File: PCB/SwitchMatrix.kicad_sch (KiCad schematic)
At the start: 94 parts, among them K1 KEYSW, K10 KEYSW, K11 KEYSW, K12 KEYSW, K13 KEYSW, K14 KEYSW, K15 KEYSW, K16 KEYSW, K17 KEYSW, K18 KEYSW, K19 KEYSW, K2 KEYSW, K20 KEYSW, K21 KEYSW, K22 KEYSW, K23 KEYSW, K24 KEYSW, K25 KEYSW, K26 KEYSW, K27 KEYSW, K28 KEYSW, K29 KEYSW, K3 KEYSW, K30 KEYSW, K31 KEYSW, K32 KEYSW, K33 KEYSW, K34 KEYSW, K35 KEYSW, K36 KEYSW, K37 KEYSW, K38 KEYSW, K39 KEYSW, K4 KEYSW, K40 KEYSW, K41 KEYSW, K42 KEYSW, K43 KEYSW, K44 KEYSW, K45 KEYSW, K46 KEYSW, K47 KEYSW, K5 KEYSW, K6 KEYSW, K7 KEYSW, K8 KEYSW, K9 KEYSW

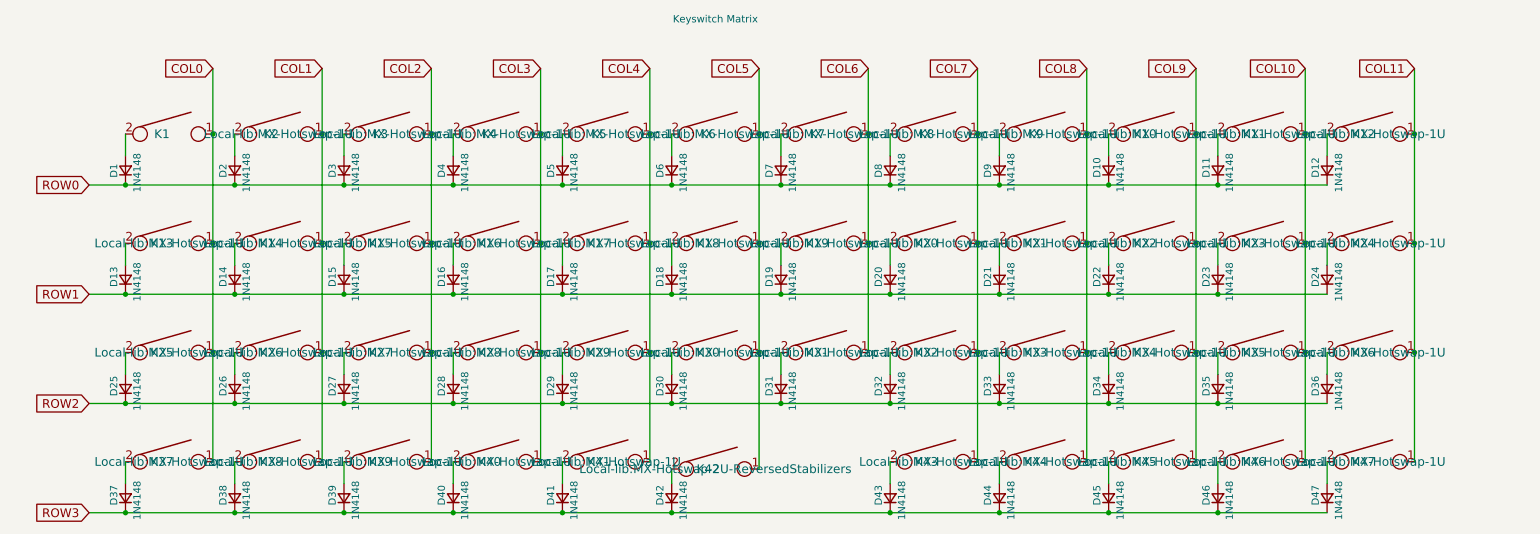
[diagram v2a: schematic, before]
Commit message: update 1u footprints adjust spacing
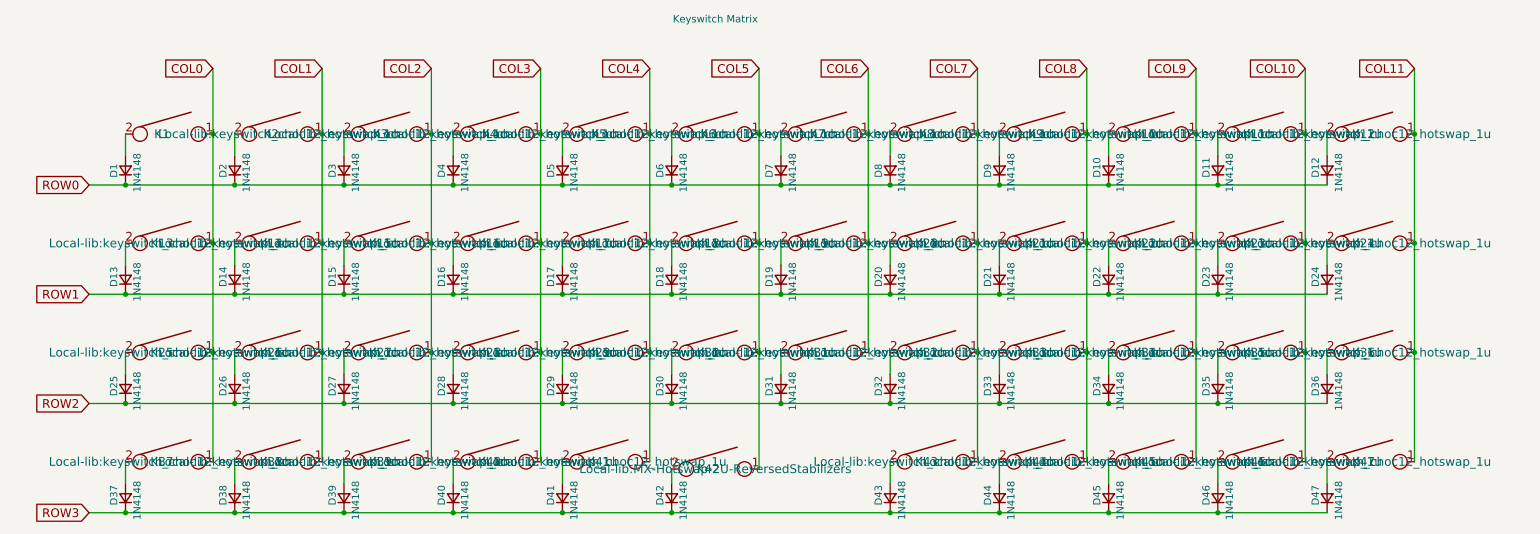
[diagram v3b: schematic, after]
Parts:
- K1, K10, K11, K12, K13, K14, K15, K16, K17, K18, K19, K2, K20, K21, K22, K23, K24, K25, K26, K27, K28, K29, K3, K30, K31, K32, K33, K34, K35, K36, K37, K38, K39, K4, K40, K41, K43, K44, K45, K46, K47, K5, K6, K7, K8, K9: footprint Local-lib:MX-Hotswap-1U -> Local-lib:keyswitch_choc12_hotswap_1u
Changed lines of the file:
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@@
 			)
 		)
-		(property "Footprint" "Local-lib:MX-Hotswap-1U"
+		(property "Footprint" "Local-lib:keyswitch_choc12_hotswap_1u"
 			(at 204.47 124.46 0)
 			(show_name no)
@@
 			)
 		)
-		(property "Footprint" "Local-lib:MX-Hotswap-1U"
+		(property "Footprint" "Local-lib:keyswitch_choc12_hotswap_1u"
 			(at 90.17 105.41 0)
 			(show_name no)
@@
 			)
 		)
-		(property "Footprint" "Local-lib:MX-Hotswap-1U"
+		(property "Footprint" "Local-lib:keyswitch_choc12_hotswap_1u"
 			(at 166.37 105.41 0)
 			(show_name no)
@@
 			)
 		)
-		(property "Footprint" "Local-lib:MX-Hotswap-1U"
+		(property "Footprint" "Local-lib:keyswitch_choc12_hotswap_1u"
 			(at 90.17 86.36 0)
 			(show_name no)
@@
 			)
 		)
-		(property "Footprint" "Local-lib:MX-Hotswap-1U"
+		(property "Footprint" "Local-lib:keyswitch_choc12_hotswap_1u"
 			(at 52.07 86.36 0)
 			(show_name no)
@@
 			)
 		)
-		(property "Footprint" "Local-lib:MX-Hotswap-1U"
+		(property "Footprint" "Local-lib:keyswitch_choc12_hotswap_1u"
 			(at 261.62 105.41 0)
 			(show_name no)
@@
 			)
 		)
-		(property "Footprint" "Local-lib:MX-Hotswap-1U"
+		(property "Footprint" "Local-lib:keyswitch_choc12_hotswap_1u"
 			(at 71.12 67.31 0)
 			(show_name no)
@@
 			)
 		)
-		(property "Footprint" "Local-lib:MX-Hotswap-1U"
+		(property "Footprint" "Local-lib:keyswitch_choc12_hotswap_1u"
 			(at 147.32 86.36 0)
 			(show_name no)
@@
 			)
 		)
-		(property "Footprint" "Local-lib:MX-Hotswap-1U"
+		(property "Footprint" "Local-lib:keyswitch_choc12_hotswap_1u"
 			(at 71.12 124.46 0)
 			(show_name no)
@@
 			)
 		)
-		(property "Footprint" "Local-lib:MX-Hotswap-1U"
+		(property "Footprint" "Local-lib:keyswitch_choc12_hotswap_1u"
 			(at 52.07 105.41 0)
 			(show_name no)
@@
 			)
 		)
-		(property "Footprint" "Local-lib:MX-Hotswap-1U"
+		(property "Footprint" "Local-lib:keyswitch_choc12_hotswap_1u"
 			(at 128.27 124.46 0)
 			(show_name no)
@@
 			)
 		)
-		(property "Footprint" "Local-lib:MX-Hotswap-1U"
+		(property "Footprint" "Local-lib:keyswitch_choc12_hotswap_1u"
 			(at 90.17 67.31 0)
 			(show_name no)
@@
 			)
 		)
-		(property "Footprint" "Local-lib:MX-Hotswap-1U"
+		(property "Footprint" "Local-lib:keyswitch_choc12_hotswap_1u"
 			(at 147.32 105.41 0)
 			(show_name no)
@@
 			)
 		)
-		(property "Footprint" "Local-lib:MX-Hotswap-1U"
+		(property "Footprint" "Local-lib:keyswitch_choc12_hotswap_1u"
 			(at 109.22 86.36 0)
 			(show_name no)
@@
 			)
 		)
-		(property "Footprint" "Local-lib:MX-Hotswap-1U"
+		(property "Footprint" "Local-lib:keyswitch_choc12_hotswap_1u"
 			(at 185.42 124.46 0)
 			(show_name no)
@@
 			)
 		)
-		(property "Footprint" "Local-lib:MX-Hotswap-1U"
+		(property "Footprint" "Local-lib:keyswitch_choc12_hotswap_1u"
 			(at 185.42 86.36 0)
 			(show_name no)
@@
 			)
 		)
-		(property "Footprint" "Local-lib:MX-Hotswap-1U"
+		(property "Footprint" "Local-lib:keyswitch_choc12_hotswap_1u"
 			(at 223.52 105.41 0)
 			(show_name no)
@@
 			)
 		)
-		(property "Footprint" "Local-lib:MX-Hotswap-1U"
+		(property "Footprint" "Local-lib:keyswitch_choc12_hotswap_1u"
 			(at 242.57 86.36 0)
 			(show_name no)
@@
 			)
 		)
-		(property "Footprint" "Local-lib:MX-Hotswap-1U"
+		(property "Footprint" "Local-lib:keyswitch_choc12_hotswap_1u"
 			(at 147.32 67.31 0)
 			(show_name no)
@@
 			)
 		)
-		(property "Footprint" "Local-lib:MX-Hotswap-1U"
+		(property "Footprint" "Local-lib:keyswitch_choc12_hotswap_1u"
 			(at 71.12 105.41 0)
 			(show_name no)
@@
 			)
 		)
-		(property "Footprint" "Local-lib:MX-Hotswap-1U"
+		(property "Footprint" "Local-lib:keyswitch_choc12_hotswap_1u"
 			(at 109.22 124.46 0)
 			(show_name no)
@@
 			)
 		)
-		(property "Footprint" "Local-lib:MX-Hotswap-1U"
+		(property "Footprint" "Local-lib:keyswitch_choc12_hotswap_1u"
 			(at 128.27 67.31 0)
 			(show_name no)
@@
 			)
 		)
-		(property "Footprint" "Local-lib:MX-Hotswap-1U"
+		(property "Footprint" "Local-lib:keyswitch_choc12_hotswap_1u"
 			(at 261.62 124.46 0)
 			(show_name no)
@@
 			)
 		)
-		(property "Footprint" "Local-lib:MX-Hotswap-1U"
+		(property "Footprint" "Local-lib:keyswitch_choc12_hotswap_1u"
 			(at 242.57 67.31 0)
 			(show_name no)
@@
 			)
 		)
-		(property "Footprint" "Local-lib:MX-Hotswap-1U"
+		(property "Footprint" "Local-lib:keyswitch_choc12_hotswap_1u"
 			(at 185.42 67.31 0)
 			(show_name no)
@@
 			)
 		)
-		(property "Footprint" "Local-lib:MX-Hotswap-1U"
+		(property "Footprint" "Local-lib:keyswitch_choc12_hotswap_1u"
 			(at 109.22 67.31 0)
 			(show_name no)
@@
 			)
 		)
-		(property "Footprint" "Local-lib:MX-Hotswap-1U"
+		(property "Footprint" "Local-lib:keyswitch_choc12_hotswap_1u"
 			(at 128.27 105.41 0)
 			(show_name no)
@@
 			)
 		)
-		(property "Footprint" "Local-lib:MX-Hotswap-1U"
+		(property "Footprint" "Local-lib:keyswitch_choc12_hotswap_1u"
 			(at 204.47 86.36 0)
 			(show_name no)
@@
 			)
 		)
-		(property "Footprint" "Local-lib:MX-Hotswap-1U"
+		(property "Footprint" "Local-lib:keyswitch_choc12_hotswap_1u"
 			(at 109.22 105.41 0)
 			(show_name no)
@@
 			)
 		)
-		(property "Footprint" "Local-lib:MX-Hotswap-1U"
+		(property "Footprint" "Local-lib:keyswitch_choc12_hotswap_1u"
 			(at 261.62 86.36 0)
 			(show_name no)
@@
 			)
 		)
-		(property "Footprint" "Local-lib:MX-Hotswap-1U"
+		(property "Footprint" "Local-lib:keyswitch_choc12_hotswap_1u"
 			(at 52.07 67.31 0)
 			(hide yes)
@@
 			)
 		)
-		(property "Footprint" "Local-lib:MX-Hotswap-1U"
+		(property "Footprint" "Local-lib:keyswitch_choc12_hotswap_1u"
 			(at 242.57 105.41 0)
 			(show_name no)
@@
 			)
 		)
-		(property "Footprint" "Local-lib:MX-Hotswap-1U"
+		(property "Footprint" "Local-lib:keyswitch_choc12_hotswap_1u"
 			(at 166.37 67.31 0)
 			(show_name no)
@@
 			)
 		)
-		(property "Footprint" "Local-lib:MX-Hotswap-1U"
+		(property "Footprint" "Local-lib:keyswitch_choc12_hotswap_1u"
 			(at 242.57 124.46 0)
 			(show_name no)
@@
 			)
 		)
-		(property "Footprint" "Local-lib:MX-Hotswap-1U"
+		(property "Footprint" "Local-lib:keyswitch_choc12_hotswap_1u"
 			(at 128.27 86.36 0)
 			(show_name no)
@@
 			)
 		)
-		(property "Footprint" "Local-lib:MX-Hotswap-1U"
+		(property "Footprint" "Local-lib:keyswitch_choc12_hotswap_1u"
 			(at 223.52 124.46 0)
 			(show_name no)
@@
 			)
 		)
-		(property "Footprint" "Local-lib:MX-Hotswap-1U"
+		(property "Footprint" "Local-lib:keyswitch_choc12_hotswap_1u"
 			(at 223.52 86.36 0)
 			(show_name no)
@@
 			)
 		)
-		(property "Footprint" "Local-lib:MX-Hotswap-1U"
+		(property "Footprint" "Local-lib:keyswitch_choc12_hotswap_1u"
 			(at 204.47 105.41 0)
 			(show_name no)
@@
 			)
 		)
-		(property "Footprint" "Local-lib:MX-Hotswap-1U"
+		(property "Footprint" "Local-lib:keyswitch_choc12_hotswap_1u"
 			(at 166.37 86.36 0)
 			(show_name no)
@@
 			)
 		)
-		(property "Footprint" "Local-lib:MX-Hotswap-1U"
+		(property "Footprint" "Local-lib:keyswitch_choc12_hotswap_1u"
 			(at 52.07 124.46 0)
 			(show_name no)
@@
 			)
 		)
-		(property "Footprint" "Local-lib:MX-Hotswap-1U"
+		(property "Footprint" "Local-lib:keyswitch_choc12_hotswap_1u"
 			(at 185.42 105.41 0)
 			(show_name no)
@@
 			)
 		)
-		(property "Footprint" "Local-lib:MX-Hotswap-1U"
+		(property "Footprint" "Local-lib:keyswitch_choc12_hotswap_1u"
 			(at 223.52 67.31 0)
 			(show_name no)
@@
 			)
 		)
-		(property "Footprint" "Local-lib:MX-Hotswap-1U"
+		(property "Footprint" "Local-lib:keyswitch_choc12_hotswap_1u"
 			(at 71.12 86.36 0)
 			(show_name no)
@@
 			)
 		)
-		(property "Footprint" "Local-lib:MX-Hotswap-1U"
+		(property "Footprint" "Local-lib:keyswitch_choc12_hotswap_1u"
 			(at 90.17 124.46 0)
 			(show_name no)
@@
 			)
 		)
-		(property "Footprint" "Local-lib:MX-Hotswap-1U"
+		(property "Footprint" "Local-lib:keyswitch_choc12_hotswap_1u"
 			(at 204.47 67.31 0)
 			(show_name no)
@@
 			)
 		)
-		(property "Footprint" "Local-lib:MX-Hotswap-1U"
+		(property "Footprint" "Local-lib:keyswitch_choc12_hotswap_1u"
 			(at 261.62 67.31 0)
 			(show_name no)
